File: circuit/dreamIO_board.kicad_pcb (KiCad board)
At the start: 2 copper layers, 85 parts, among them IC1 TPS61200, P1 BATT, P2 CONN_01X06, P3 CONN_01X06, P4 CONN_01X02, P5 CONN_01X06, P6 CONN_01X02, P7 CONN_01X03, P8 CONN_01X04, P9 PixelOut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

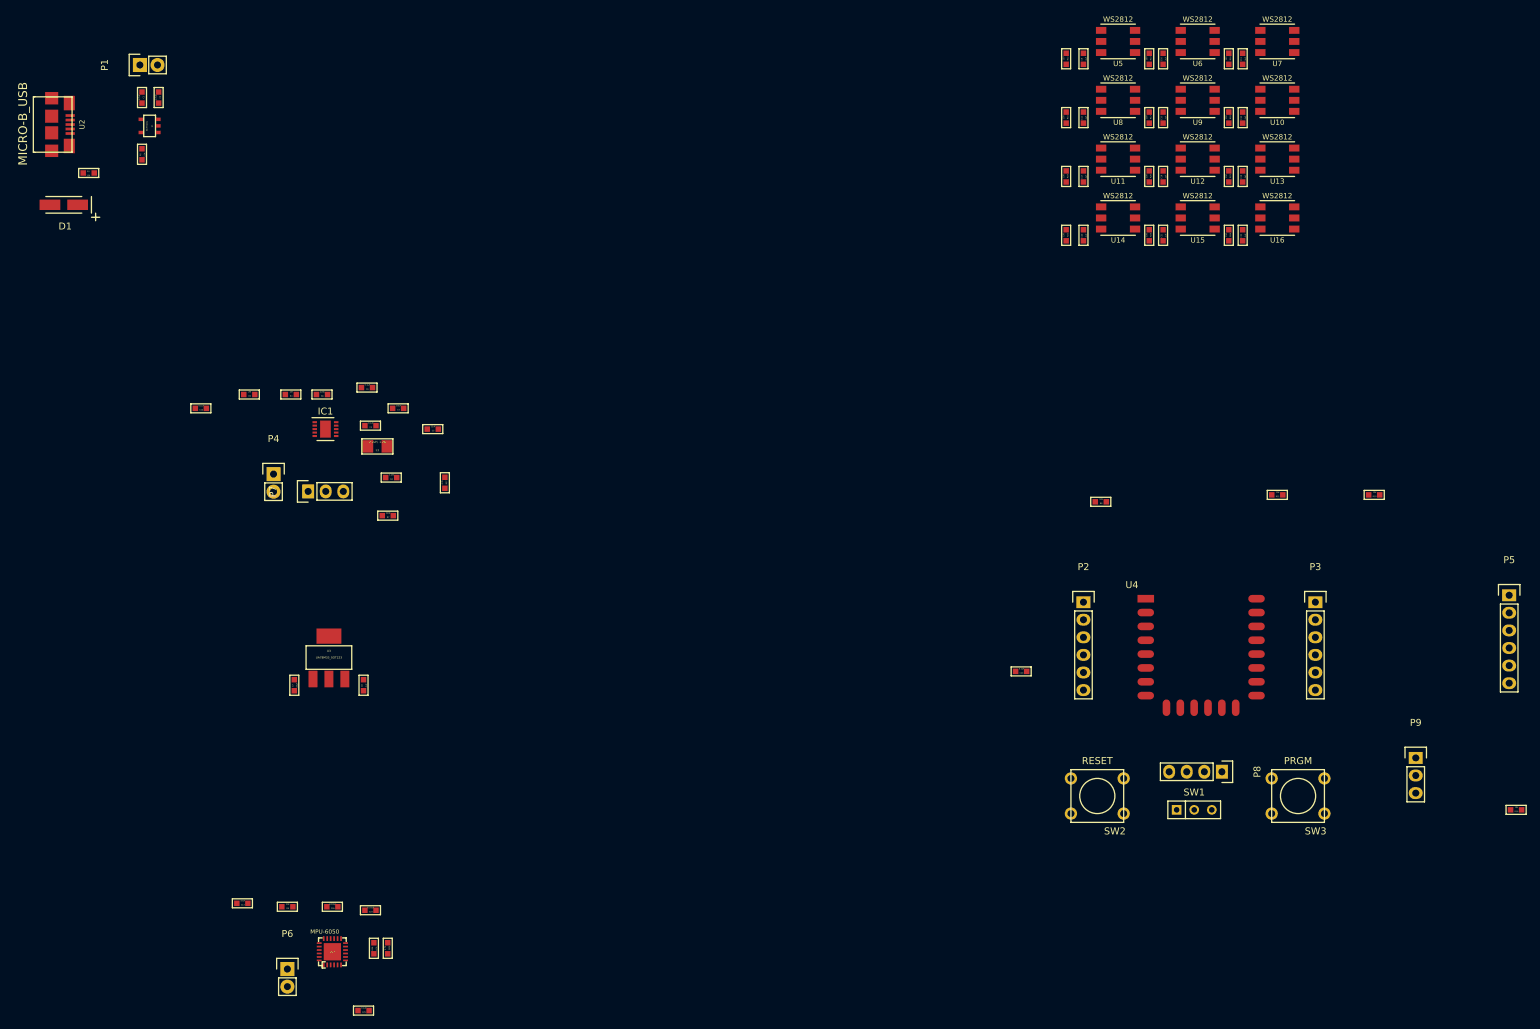
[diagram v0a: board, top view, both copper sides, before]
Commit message: fixed IC1 footprint
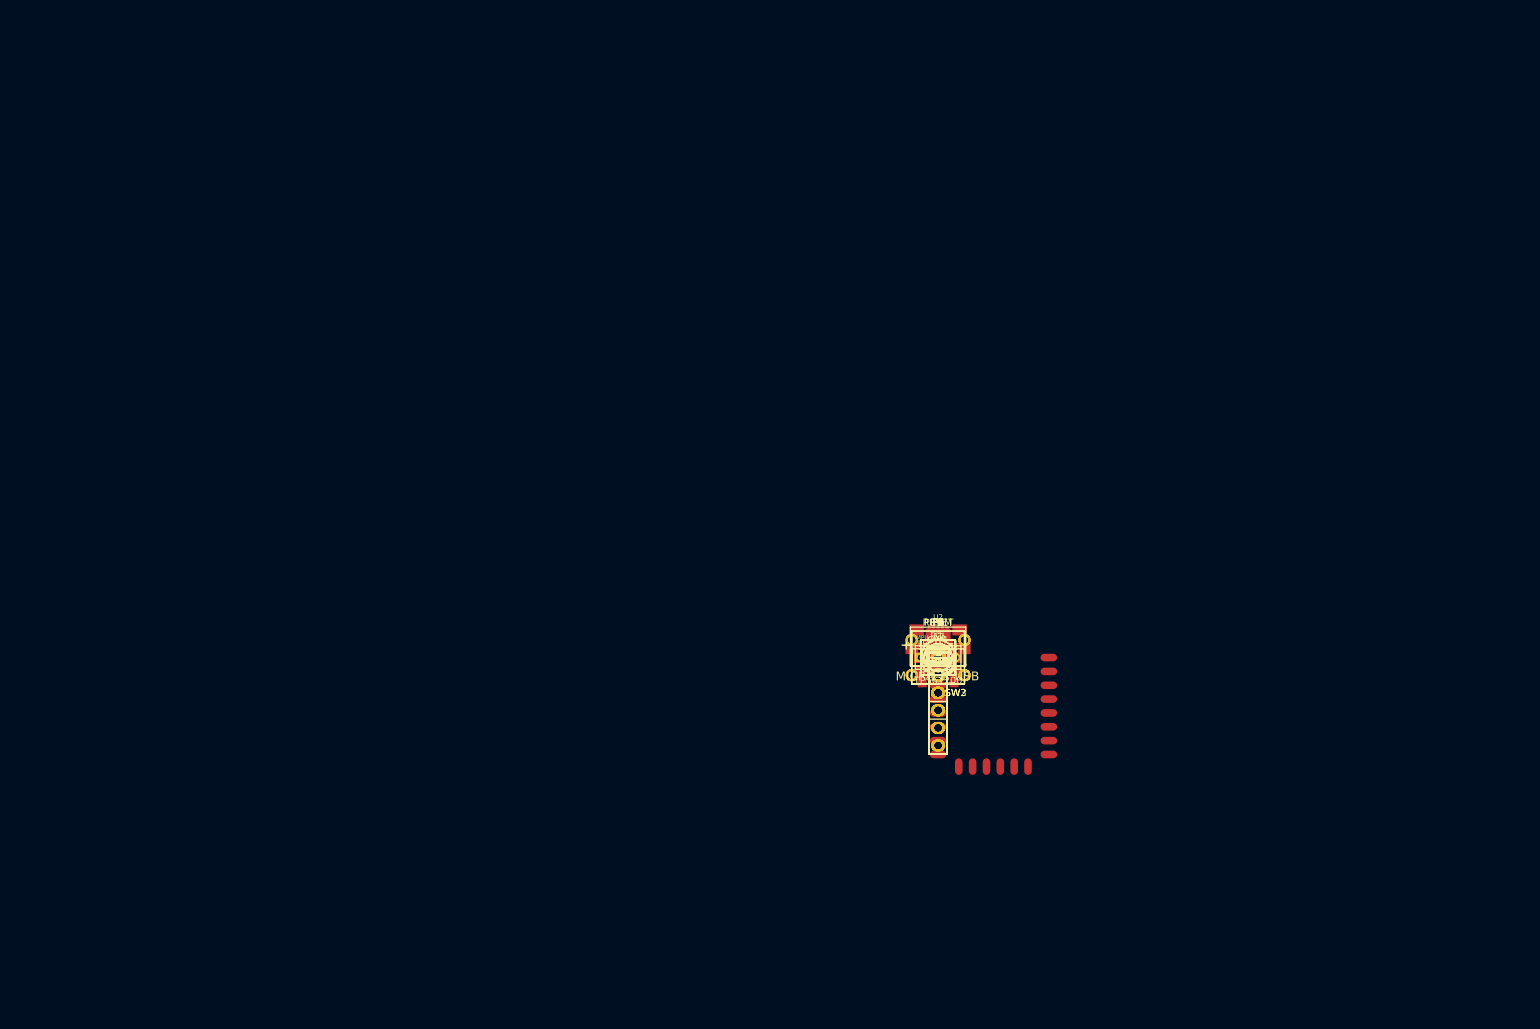
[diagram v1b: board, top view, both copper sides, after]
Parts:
- removed R13, R14, R15, R17, R18, R19, R20, R21, R22, R23, R24: 150, kicad-libraries:0603
- removed U10, U11, U12, U13, U14, U15, U16, U5, U6, U7, U8, U9: WS2812, shardy:5050
- added LED1, LED10, LED11, LED12, LED2, LED3, LED4, LED5, LED6, LED7, LED8, LED9: WS2812B, kicad-libraries:WS2812B_LED, F.Cu at (148.5, 105.0)
- IC1: footprint Housings_DFN_QFN:DFN-10-1EP_3x3mm_Pitch0.5mm -> tps61200_qfn_custom:tps61200_QFN-10_PAD
- R12: value 150 -> 220
- moved U2 150.7 mm to (148.5, 105.0), turned to 0 degrees
- moved P1 143.6 mm to (148.5, 105.0), turned to 0 degrees
- moved D1 142.2 mm to (148.5, 105.0), turned to 0 degrees
- moved R1 141.3 mm to (148.5, 105.0), turned to 0 degrees
- moved C1 140.6 mm to (148.5, 105.0), turned to 0 degrees
- moved C2 138.7 mm to (148.5, 105.0), turned to 0 degrees
- moved U1 137.4 mm to (148.5, 105.0), turned to 0 degrees
- moved R2 136.1 mm to (148.5, 105.0), turned to 0 degrees
- moved C24 112.4 mm to (148.5, 105.0)
- moved C13 106.6 mm to (148.5, 105.0)
- moved R5 106.5 mm to (148.5, 105.0)
- moved P6 104.2 mm to (148.5, 105.0)
- moved R3 100.9 mm to (148.5, 105.0)
- moved R9 100.7 mm to (148.5, 105.0)
- moved P4 99.6 mm to (148.5, 105.0)
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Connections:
- C10 pad 1: Net-(C10-Pad1) -> GND
- C10 pad 2: GND -> VCC
- C11 pad 1: Net-(C11-Pad1) -> GND
- C11 pad 2: GND -> VCC
- C12 pad 1: Net-(C12-Pad1) -> GND
- C12 pad 2: GND -> VCC
- C15 pad 1: Net-(C15-Pad1) -> GND
- C15 pad 2: GND -> VCC
- C16 pad 1: Net-(C16-Pad1) -> GND
- C16 pad 2: GND -> VCC
- C17 pad 1: Net-(C17-Pad1) -> GND
- C17 pad 2: GND -> VCC
- C18 pad 1: Net-(C18-Pad1) -> GND
- C18 pad 2: GND -> VCC
- C19 pad 1: Net-(C19-Pad1) -> GND
- C19 pad 2: GND -> VCC
- C20 pad 1: Net-(C20-Pad1) -> GND
- C20 pad 2: GND -> VCC
- C21 pad 1: Net-(C21-Pad1) -> GND
- C21 pad 2: GND -> VCC
- C22 pad 1: Net-(C22-Pad1) -> GND
- C22 pad 2: GND -> VCC
- C9 pad 1: Net-(C9-Pad1) -> GND
- C9 pad 2: GND -> VCC
- R12 pad 1: VCC -> Net-(LED1-Pad4)
- R12 pad 2: Net-(C9-Pad1) -> GPIO15
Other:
- rule pad_to_mask_clearance: 0.2 -> 0

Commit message: grouped PCB components together for board:
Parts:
- D1: footprint Capacitors_Tantalum_SMD:TantalC_SizeA_EIA-3216_HandSoldering -> kicad-libraries:0603
- moved LED1 154.3 mm to (22.0, 16.6), turned to 180 degrees
- moved LED10 154.3 mm to (16.9, 24.4), turned to 270 degrees
- moved R12 154.0 mm to (20.0, 20.2)
- moved C20 152.6 mm to (20.2, 22.4), turned to 90 degrees
- moved C9 150.6 mm to (24.0, 20.2)
- moved LED11 148.3 mm to (16.8, 36.8), turned to 270 degrees
- moved C21 146.3 mm to (20.2, 34.8), turned to 90 degrees
- moved LED12 143.0 mm to (16.7, 49.6), turned to 270 degrees
- moved LED2 142.3 mm to (36.8, 16.8), turned to 180 degrees
- moved C23 142.1 mm to (261.6, 19.0), turned to 270 degrees
- moved C24 141.1 mm to (260.4, 19.0), turned to 270 degrees
- moved C25 141.0 mm to (263.0, 22.8)
- moved C22 140.7 mm to (20.0, 47.6), turned to 90 degrees
- moved C10 138.7 mm to (38.8, 20.2)
- moved U17 137.6 mm to (259.0, 23.0)
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
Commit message: finished layout
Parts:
- removed P8: CONN_01X04, Pin_Headers:Pin_Header_Straight_1x04
- added H4: SCREWHOLE, shardy:1pin, F.Cu at (69.3, 68.7)
- added H4: SCREWHOLE, shardy:1pin, F.Cu at (19.3, 68.7)
- added H4: SCREWHOLE, shardy:1pin, F.Cu at (69.3, 18.7)
- added H4: SCREWHOLE, shardy:1pin, F.Cu at (19.3, 18.7)
- C1, C2, C3, C4, C5, C6, C7, C8, D1, IC1, L1, R1, R2, R3, R4, R5, R6, R7, U1, U2, U3: moved to B.Cu
- P2, P3: value CONN_01X06 -> CONN_01X08; footprint Pin_Headers:Pin_Header_Straight_1x06 -> _connectors:_Pin2mm_8
- P4: footprint Pin_Headers:Pin_Header_Straight_1x02 -> _connectors:_Solder_Pad2.54_2; moved to B.Cu
- P5: footprint Pin_Headers:Pin_Header_Straight_1x06 -> _connectors:_Pin2mm_6
- P6: value CONN_01X02 -> gnd_con; footprint Pin_Headers:Pin_Header_Straight_1x02 -> _connectors:_Solder_Pad2.54_2
- P7: footprint Pin_Headers:Pin_Header_Straight_1x03 -> _connectors:_Solder_Pad2.54_3; moved to B.Cu
- SW2, SW3: footprint shardy:SW_PUSH_SMALL -> kicad-libraries:SW_06_SMD
- moved C25 234.8 mm to (31.6, 62.4)
- moved R27 231.7 mm to (27.4, 60.1), turned to 180 degrees
- moved R25 230.2 mm to (27.4, 58.7), turned to 0 degrees
- moved U17 230.1 mm to (31.7, 58.7), turned to 270 degrees
- moved C23 230.0 mm to (35.7, 62.3), turned to 180 degrees
- moved R26 228.6 mm to (27.4, 57.3), turned to 0 degrees
- moved C24 228.6 mm to (35.7, 60.9), turned to 180 degrees
- moved C26 225.7 mm to (31.7, 55.2)
- moved P9 203.7 mm to (21.8, 35.7), turned to 270 degrees
- moved P6 129.7 mm to (25.5, 41.3), turned to 180 degrees
- moved P7 128.3 mm to (23.3, 50.3), turned to 0 degrees
- moved R7 124.4 mm to (26.6, 45.8), turned to 270 degrees
- moved C4 124.2 mm to (29.9, 43.1), turned to 270 degrees
- moved C5 124.1 mm to (29.1, 40.8), turned to 0 degrees
- moved R6 123.9 mm to (25.1, 45.8), turned to 270 degrees
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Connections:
- P2 pad 1: ADC -> RESET
- P2 pad 2: GPIO0 -> ADC
- P2 pad 3: GPIO2 -> CH_PD
- P2 pad 4: GPIO4 -> GPIO16
- P2 pad 5: GPIO5 -> GPIO14
- P2 pad 6: GPIO9 -> GPIO12
- P3 pad 1: GPIO16 -> TX
- P3 pad 2: GPIO15 -> RX
- P3 pad 3: GPIO14 -> GPIO5
- P3 pad 4: GPIO13 -> GPIO4
- P3 pad 5: GPIO12 -> GPIO0
- P3 pad 6: GPIO10 -> GPIO2
- P5 pad 1: Net-(P5-Pad1) -> CS0
- P5 pad 2: TX -> MISO
- P5 pad 3: RX -> GPIO9
- P5 pad 4: VCC -> GPIO10
- P5 pad 5: GND -> MOSI
- P5 pad 6: +3V3 -> SCLK
- R8 pad 2: Net-(R8-Pad2) -> CH_PD
- R9 pad 2: Net-(R9-Pad2) -> RESET
- SW1 pad 3: Net-(SW1-Pad3) -> (no net)
- SW2 pad 2: Net-(R9-Pad2) -> RESET
- U17 pad 14: Net-(U17-Pad14) -> (no net)
- U17 pad 15: Net-(U17-Pad15) -> (no net)
- U17 pad 16: Net-(U17-Pad16) -> (no net)
- U17 pad 17: Net-(U17-Pad17) -> (no net)
- U17 pad 19: Net-(U17-Pad19) -> (no net)
- U17 pad 2: Net-(U17-Pad2) -> (no net)
- U17 pad 21: Net-(U17-Pad21) -> (no net)
- U17 pad 22: Net-(U17-Pad22) -> (no net)
- U17 pad 3: Net-(U17-Pad3) -> (no net)
- U17 pad 4: Net-(U17-Pad4) -> (no net)
- U17 pad 5: Net-(U17-Pad5) -> (no net)
- U17 pad 6: XDA -> (no net)
- U17 pad 7: XCL -> (no net)
- U2 pad 2: Net-(U2-Pad2) -> (no net)
- U2 pad 3: Net-(U2-Pad3) -> (no net)
- U2 pad 4: Net-(U2-Pad4) -> (no net)
- U4 pad 1: Net-(R9-Pad2) -> RESET
- U4 pad 3: Net-(R8-Pad2) -> CH_PD
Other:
- board outline added: 60 x 60 mm
